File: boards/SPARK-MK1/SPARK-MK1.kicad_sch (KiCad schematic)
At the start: 64 parts, among them J1 Screw_Terminal_01x02, J101 Conn_01x04_Pin, J102 Screw_Terminal_01x02, J103 Screw_Terminal_01x02, J104 Conn_01x04_Pin, J105 Conn_01x04_Pin, J106 Screw_Terminal_01x02, J107 Screw_Terminal_01x02, J108 Conn_01x04_Pin, J109 Conn_01x04_Pin, J110 Conn_01x02_Pin, J111 Conn_01x04_Pin, J112 Conn_01x04_Pin, J2 Screw_Terminal_01x02, J3 Screw_Terminal_01x02, J4 Screw_Terminal_01x02, U1 AD5252BRUZ1, U101 AD5252BRUZ1, U2 Teensy4.1_bare, U5 TPS25947, U6 TPS25947, U7 TPS25947, U8 TPS25947

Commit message: Fixing Footprints, etc
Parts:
- U2: footprint Teensy4.1bare:Teensy41_bare_pins -> Teensy4.1bare:Teensy_4.1
- U5, U6, U7, U8: footprint efuse:VQFN-HR-RPW0010A -> Package_VQFN:VQFN-HR-RPW0010A
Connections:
- no-connect marks 8 -> 37
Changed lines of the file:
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@@
   (junction (at 297.18 138.43) (diameter 0) (color 0 0 0 0)
   )
+  (no_connect (at 110.49 135.89))
+  (no_connect (at 110.49 168.91))
+  (no_connect (at 54.61 151.13))
   (no_connect (at 30.48 43.18))
+  (no_connect (at 110.49 146.05))
+  (no_connect (at 110.49 181.61))
+  (no_connect (at 54.61 163.83))
   (no_connect (at 105.41 41.91))
   (no_connect (at 321.31 97.79))
   (no_connect (at 30.48 45.72))
+  (no_connect (at 110.49 176.53))
+  (no_connect (at 54.61 156.21))
+  (no_connect (at 110.49 158.75))
+  (no_connect (at 110.49 143.51))
+  (no_connect (at 110.49 184.15))
+  (no_connect (at 110.49 179.07))
+  (no_connect (at 54.61 166.37))
+  (no_connect (at 110.49 166.37))
+  (no_connect (at 54.61 171.45))
   (no_connect (at 320.04 41.91))
+  (no_connect (at 110.49 171.45))
+  (no_connect (at 110.49 140.97))
   (no_connect (at 105.41 44.45))
+  (no_connect (at 54.61 148.59))
+  (no_connect (at 110.49 173.99))
   (no_connect (at 320.04 151.13))
   (no_connect (at 318.77 204.47))
+  (no_connect (at 110.49 133.35))
+  (no_connect (at 110.49 156.21))
+  (no_connect (at 54.61 168.91))
+  (no_connect (at 110.49 138.43))
+  (no_connect (at 54.61 184.15))
+  (no_connect (at 110.49 163.83))
+  (no_connect (at 110.49 121.92))
+  (no_connect (at 54.61 158.75))
+  (no_connect (at 110.49 125.73))
+  (no_connect (at 54.61 153.67))
   (wire (pts (xy 318.77 39.37) (xy 320.04 39.37))
     (stroke (width 0) (type default))
@@
       (effects (font (size 1.27 1.27)))
     )
-    (property "Footprint" "efuse:VQFN-HR-RPW0010A" (at 337.82 105.41 0)
+    (property "Footprint" "Package_VQFN:VQFN-HR-RPW0010A" (at 337.82 105.41 0)
       (effects (font (size 1.27 1.27)) hide)
     )
@@
       (effects (font (size 1.27 1.27)))
     )
-    (property "Footprint" "Teensy4.1bare:Teensy41_bare_pins" (at 82.55 194.31 0)
+    (property "Footprint" "Teensy4.1bare:Teensy_4.1" (at 82.55 194.31 0)
       (effects (font (size 1.27 1.27)) hide)
     )
@@
       (effects (font (size 1.27 1.27)))
     )
-    (property "Footprint" "efuse:VQFN-HR-RPW0010A" (at 335.28 212.09 0)
+    (property "Footprint" "Package_VQFN:VQFN-HR-RPW0010A" (at 335.28 212.09 0)
       (effects (font (size 1.27 1.27)) hide)
     )
@@
       (effects (font (size 1.27 1.27)))
     )
-    (property "Footprint" "efuse:VQFN-HR-RPW0010A" (at 336.55 158.75 0)
+    (property "Footprint" "Package_VQFN:VQFN-HR-RPW0010A" (at 336.55 158.75 0)
       (effects (font (size 1.27 1.27)) hide)
     )
@@
       (effects (font (size 1.27 1.27)))
     )
-    (property "Footprint" "efuse:VQFN-HR-RPW0010A" (at 336.55 49.53 0)
+    (property "Footprint" "Package_VQFN:VQFN-HR-RPW0010A" (at 336.55 49.53 0)
       (effects (font (size 1.27 1.27)) hide)
     )

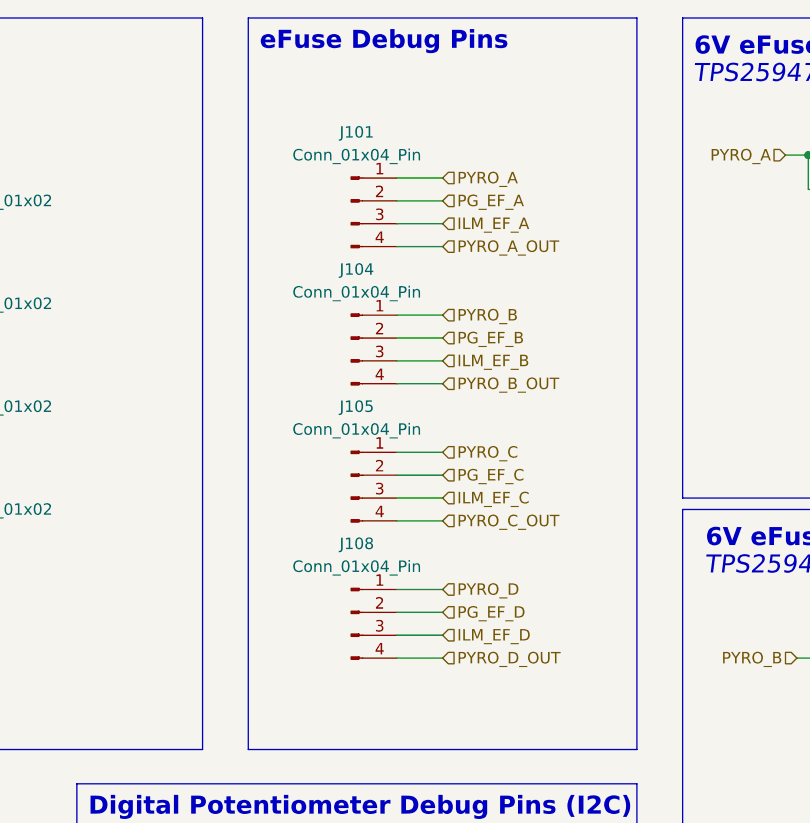
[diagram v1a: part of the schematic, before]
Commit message: Four pins -> three pins
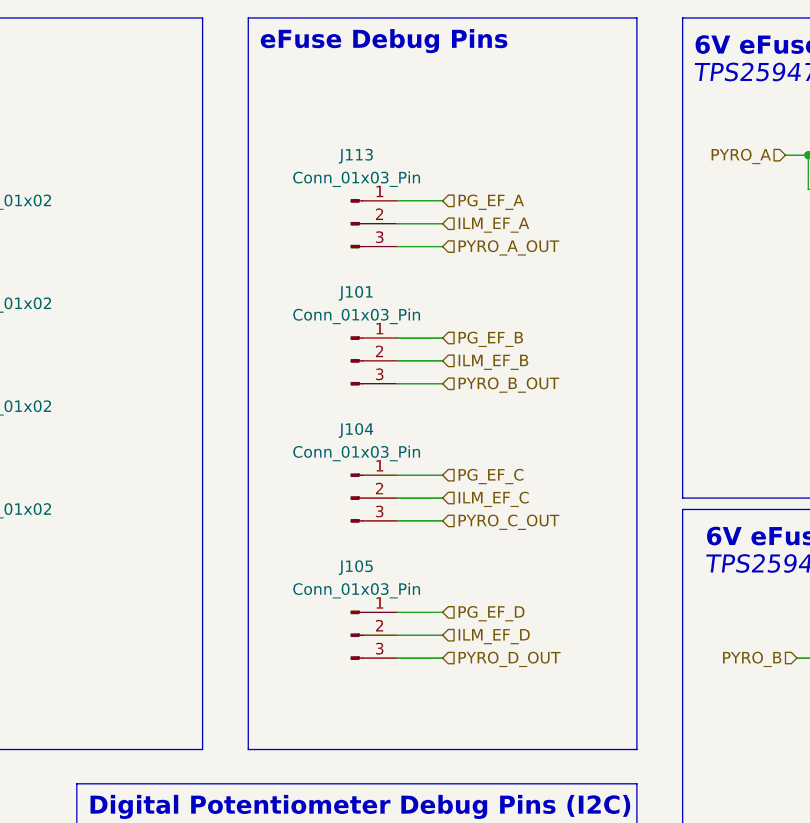
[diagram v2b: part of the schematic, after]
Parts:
- removed J101, J104, J105, J108: Conn_01x04_Pin, Connector_PinHeader_2.54mm:PinHeader_1x04_P2.54mm_Vertical, symbol Connector:Conn_01x04_Pin
- added J101, J104, J105, J113: Conn_01x03_Pin, Connector_PinHeader_2.54mm:PinHeader_1x03_P2.54mm_Vertical, symbol Connector:Conn_01x03_Pin
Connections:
- net B1_A: now also J113.2 (Pin_2)
- net B1_B: now also J104.2 (Pin_2)
- net B3_A: now also J101.2 (Pin_2)
- net B3_B: now also J105.2 (Pin_2)
- net GND: now also J101.3 (Pin_3), J104.3 (Pin_3), J105.3 (Pin_3), J113.3 (Pin_3)
- net PG_EF_A: now also J113.1 (Pin_1)
- net PG_EF_B: now also J101.1 (Pin_1)
- net PG_EF_C: now also J104.1 (Pin_1)
- net PG_EF_D: now also J105.1 (Pin_1)
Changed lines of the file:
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@@
     (stroke (width 0) (type default))
   )
-  (wire (pts (xy 251.46 31.75) (xy 256.54 31.75))
-    (stroke (width 0) (type default))
-  )
   (wire (pts (xy 336.55 46.99) (xy 336.55 53.34))
     (stroke (width 0) (type default))
@@
     (stroke (width 0) (type default))
   )
-  (wire (pts (xy 251.46 77.47) (xy 256.54 77.47))
-    (stroke (width 0) (type default))
-  )
   (wire (pts (xy 384.81 138.43) (xy 392.43 138.43))
     (stroke (width 0) (type default))
@@
     (stroke (width 0) (type default))
   )
-  (wire (pts (xy 251.46 46.99) (xy 256.54 46.99))
-    (stroke (width 0) (type default))
-  )
   (wire (pts (xy 363.22 167.64) (xy 360.68 167.64))
     (stroke (width 0) (type default))
@@
     (stroke (width 0) (type default))
   )
-  (wire (pts (xy 251.46 62.23) (xy 256.54 62.23))
-    (stroke (width 0) (type default))
-  )
   (wire (pts (xy 259.08 115.57) (xy 264.16 115.57))
     (stroke (width 0) (type default))
@@
     (effects (font (size 1.27 1.27)) (justify left))
   )
-  (hierarchical_label "PYRO_D" (shape input) (at 256.54 77.47 0) (fields_autoplaced)
-    (effects (font (size 1.27 1.27)) (justify left))
-  )
   (hierarchical_label "W1_A" (shape bidirectional) (at 354.33 49.53 0) (fields_autoplaced)
     (effects (font (size 1.27 1.27)) (justify left))
@@
     (effects (font (size 1.27 1.27)) (justify left))
   )
-  (hierarchical_label "PYRO_A" (shape input) (at 256.54 31.75 0) (fields_autoplaced)
-    (effects (font (size 1.27 1.27)) (justify left))
-  )
   (hierarchical_label "B1_A" (shape bidirectional) (at 354.33 44.45 0) (fields_autoplaced)
     (effects (font (size 1.27 1.27)) (justify left))
@@
     (effects (font (size 1.27 1.27)) (justify right))
   )
-  (hierarchical_label "PYRO_B" (shape input) (at 256.54 46.99 0) (fields_autoplaced)
-    (effects (font (size 1.27 1.27)) (justify left))
-  )
   (hierarchical_label "PYRO_D_OUT" (shape input) (at 256.54 85.09 0) (fields_autoplaced)
     (effects (font (size 1.27 1.27)) (justify left))
@@
     (effects (font (size 1.27 1.27)) (justify left))
   )
-  (hierarchical_label "PYRO_C" (shape input) (at 256.54 62.23 0) (fields_autoplaced)
-    (effects (font (size 1.27 1.27)) (justify left))
-  )
   (hierarchical_label "PYRO_D" (shape output) (at 181.61 66.04 180) (fields_autoplaced)
     (effects (font (size 1.27 1.27)) (justify right))
@@
     )
   )
+  (symbol (lib_id "Connector:Conn_01x03_Pin") (at 246.38 82.55 0) (unit 1)
+    (in_bom yes) (on_board yes) (dnp no) (fields_autoplaced)
+    (property "Reference" "J105" (at 247.015 74.93 0)
+      (effects (font (size 1.27 1.27)))
+    )
+    (property "Value" "Conn_01x03_Pin" (at 247.015 77.47 0)
+      (effects (font (size 1.27 1.27)))
+    )
+    (property "Footprint" "Connector_PinHeader_2.54mm:PinHeader_1x03_P2.54mm_Vertical" (at 246.38 82.55 0)
+      (effects (font (size 1.27 1.27)) hide)
+    )
+    (property "Datasheet" "~" (at 246.38 82.55 0)
+      (effects (font (size 1.27 1.27)) hide)
+    )
+    (pin "3")
+    (pin "1")
+    (pin "2")
+    (instances
+      (project "SPARK-MK1"
+        (path "/9ed31ef1-850d-4612-a113-88d01cf221f5"
+          (reference "J105") (unit 1)
+        )
+      )
+    )
+  )
   (symbol (lib_id "Device:R_US") (at 367.03 104.14 0) (unit 1)
     (in_bom yes) (on_board yes) (dnp no)
@@
     )
   )
+  (symbol (lib_id "Connector:Conn_01x03_Pin") (at 246.38 52.07 0) (unit 1)
+    (in_bom yes) (on_board yes) (dnp no) (fields_autoplaced)
+    (property "Reference" "J101" (at 247.015 44.45 0)
+      (effects (font (size 1.27 1.27)))
+    )
+    (property "Value" "Conn_01x03_Pin" (at 247.015 46.99 0)
+      (effects (font (size 1.27 1.27)))
+    )
+    (property "Footprint" "Connector_PinHeader_2.54mm:PinHeader_1x03_P2.54mm_Vertical" (at 246.38 52.07 0)
+      (effects (font (size 1.27 1.27)) hide)
+    )
+    (property "Datasheet" "~" (at 246.38 52.07 0)
+      (effects (font (size 1.27 1.27)) hide)
+    )
+    (pin "3")
+    (pin "1")
+    (pin "2")
+    (instances
+      (project "SPARK-MK1"
+        (path "/9ed31ef1-850d-4612-a113-88d01cf221f5"
+          (reference "J101") (unit 1)
+        )
+      )
+    )
+  )
   (symbol (lib_id "Device:R_US") (at 307.34 149.86 0) (unit 1)
     (in_bom yes) (on_board yes) (dnp no)
@@
     )
   )
+  (symbol (lib_id "Connector:Conn_01x03_Pin") (at 246.38 36.83 0) (unit 1)
+    (in_bom yes) (on_board yes) (dnp no) (fields_autoplaced)
+    (property "Reference" "J113" (at 247.015 29.21 0)
+      (effects (font (size 1.27 1.27)))
+    )
+    (property "Value" "Conn_01x03_Pin" (at 247.015 31.75 0)
+      (effects (font (size 1.27 1.27)))
+    )
+    (property "Footprint" "Connector_PinHeader_2.54mm:PinHeader_1x03_P2.54mm_Vertical" (at 246.38 36.83 0)
+      (effects (font (size 1.27 1.27)) hide)
+    )
+    (property "Datasheet" "~" (at 246.38 36.83 0)
+      (effects (font (size 1.27 1.27)) hide)
+    )
+    (pin "3")
+    (pin "1")
+    (pin "2")
+    (instances
+      (project "SPARK-MK1"
+        (path "/9ed31ef1-850d-4612-a113-88d01cf221f5"
+          (reference "J113") (unit 1)
+        )
+      )
+    )
+  )
   (symbol (lib_id "Device:R_US") (at 307.34 40.64 0) (unit 1)
     (in_bom yes) (on_board yes) (dnp no)
@@
     )
   )
+  (symbol (lib_id "Connector:Conn_01x03_Pin") (at 246.38 67.31 0) (unit 1)
+    (in_bom yes) (on_board yes) (dnp no) (fields_autoplaced)
+    (property "Reference" "J104" (at 247.015 59.69 0)
+      (effects (font (size 1.27 1.27)))
+    )
+    (property "Value" "Conn_01x03_Pin" (at 247.015 62.23 0)
+      (effects (font (size 1.27 1.27)))
+    )
+    (property "Footprint" "Connector_PinHeader_2.54mm:PinHeader_1x03_P2.54mm_Vertical" (at 246.38 67.31 0)
+      (effects (font (size 1.27 1.27)) hide)
+    )
+    (property "Datasheet" "~" (at 246.38 67.31 0)
+      (effects (font (size 1.27 1.27)) hide)
+    )
+    (pin "3")
+    (pin "1")
+    (pin "2")
+    (instances
+      (project "SPARK-MK1"
+        (path "/9ed31ef1-850d-4612-a113-88d01cf221f5"
+          (reference "J104") (unit 1)
+        )
+      )
+    )
+  )
   (symbol (lib_id "power:GND") (at 101.6 72.39 0) (unit 1)
     (in_bom yes) (on_board yes) (dnp no) (fields_autoplaced)
@@
     )
   )
-  (symbol (lib_id "Connector:Conn_01x04_Pin") (at 246.38 80.01 0) (unit 1)
-    (in_bom yes) (on_board yes) (dnp no)
-    (property "Reference" "J108" (at 247.015 72.39 0)
-      (effects (font (size 1.27 1.27)))
-    )
-    (property "Value" "Conn_01x04_Pin" (at 247.015 74.93 0)
-      (effects (font (size 1.27 1.27)))
-    )
-    (property "Footprint" "Connector_PinHeader_2.54mm:PinHeader_1x04_P2.54mm_Vertical" (at 246.38 80.01 0)
-      (effects (font (size 1.27 1.27)) hide)
-    )
-    (property "Datasheet" "~" (at 246.38 80.01 0)
-      (effects (font (size 1.27 1.27)) hide)
-    )
-    (pin "1")
-    (pin "4")
-    (pin "2")
-    (pin "3")
-    (instances
-      (project "SPARK-MK1"
-        (path "/9ed31ef1-850d-4612-a113-88d01cf221f5"
-          (reference "J108") (unit 1)
-        )
-      )
-    )
-  )
-  (symbol (lib_id "Connector:Conn_01x04_Pin") (at 246.38 49.53 0) (unit 1)
-    (in_bom yes) (on_board yes) (dnp no)
-    (property "Reference" "J104" (at 247.015 41.91 0)
-      (effects (font (size 1.27 1.27)))
-    )
-    (property "Value" "Conn_01x04_Pin" (at 247.015 44.45 0)
-      (effects (font (size 1.27 1.27)))
-    )
-    (property "Footprint" "Connector_PinHeader_2.54mm:PinHeader_1x04_P2.54mm_Vertical" (at 246.38 49.53 0)
-      (effects (font (size 1.27 1.27)) hide)
-    )
-    (property "Datasheet" "~" (at 246.38 49.53 0)
-      (effects (font (size 1.27 1.27)) hide)
-    )
-    (pin "1")
-    (pin "4")
-    (pin "2")
-    (pin "3")
-    (instances
-      (project "SPARK-MK1"
-        (path "/9ed31ef1-850d-4612-a113-88d01cf221f5"
-          (reference "J104") (unit 1)
-        )
-      )
-    )
-  )
   (symbol (lib_id "Connector:Screw_Terminal_01x02") (at 368.3 165.1 0) (unit 1)
     (in_bom yes) (on_board yes) (dnp no) (fields_autoplaced)
@@
     )
   )
-  (symbol (lib_id "Connector:Conn_01x04_Pin") (at 246.38 64.77 0) (unit 1)
-    (in_bom yes) (on_board yes) (dnp no)
-    (property "Reference" "J105" (at 247.015 57.15 0)
-      (effects (font (size 1.27 1.27)))
-    )
-    (property "Value" "Conn_01x04_Pin" (at 247.015 59.69 0)
-      (effects (font (size 1.27 1.27)))
-    )
-    (property "Footprint" "Connector_PinHeader_2.54mm:PinHeader_1x04_P2.54mm_Vertical" (at 246.38 64.77 0)
-      (effects (font (size 1.27 1.27)) hide)
-    )
-    (property "Datasheet" "~" (at 246.38 64.77 0)
-      (effects (font (size 1.27 1.27)) hide)
-    )
-    (pin "1")
-    (pin "4")
-    (pin "2")
-    (pin "3")
-    (instances
-      (project "SPARK-MK1"
-        (path "/9ed31ef1-850d-4612-a113-88d01cf221f5"
-          (reference "J105") (unit 1)
-        )
-      )
-    )
-  )
   (symbol (lib_id "Device:R_US") (at 365.76 48.26 0) (unit 1)
     (in_bom yes) (on_board yes) (dnp no)
@@
         )
       )
-    )
-  )
-  (symbol (lib_id "Connector:Conn_01x04_Pin") (at 246.38 34.29 0) (unit 1)
-    (in_bom yes) (on_board yes) (dnp no)
-    (property "Reference" "J101" (at 247.015 26.67 0)
-      (effects (font (size 1.27 1.27)))
-    )
-    (property "Value" "Conn_01x04_Pin" (at 247.015 29.21 0)
-      (effects (font (size 1.27 1.27)))
-    )
-    (property "Footprint" "Connector_PinHeader_2.54mm:PinHeader_1x04_P2.54mm_Vertical" (at 246.38 34.29 0)
-      (effects (font (size 1.27 1.27)) hide)
-    )
-    (property "Datasheet" "~" (at 246.38 34.29 0)
-      (effects (font (size 1.27 1.27)) hide)
-    )
-    (pin "1")
-    (pin "4")
-    (pin "2")
-    (pin "3")
-    (instances
-      (project "SPARK-MK1"
-        (path "/9ed31ef1-850d-4612-a113-88d01cf221f5"
-          (reference "J101") (unit 1)
-        )
-      )

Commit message: fixing small things and adding footprints to PCB
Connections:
- net GND: no longer C11.1, C12.1, C7.1, C8.1, J1.1 (Pin_1), J101.3 (Pin_3), J104.3 (Pin_3), J105.3 (Pin_3), J113.3 (Pin_3), J2.1 (Pin_1), J3.1 (Pin_1), J4.1 (Pin_1), R23.2, R24.2, R35.2, R36.2, U5.6 (OUT), U6.6 (OUT), U7.6 (OUT), U8.6 (OUT)
- new net PYRO_A_OUT: C7.1, J1.1 (Pin_1), J113.3 (Pin_3), R23.2, U5.6 (OUT)
- new net PYRO_B_OUT: C8.1, J101.3 (Pin_3), J2.1 (Pin_1), R24.2, U6.6 (OUT)
- new net PYRO_C_OUT: C11.1, J104.3 (Pin_3), J3.1 (Pin_1), R35.2, U7.6 (OUT)
- new net PYRO_D_OUT: C12.1, J105.3 (Pin_3), J4.1 (Pin_1), R36.2, U8.6 (OUT)
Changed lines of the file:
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@@
   (junction (at 308.61 88.9) (diameter 0) (color 0 0 0 0)
   )
-  (junction (at 377.19 109.22) (diameter 0) (color 0 0 0 0)
-  )
   (junction (at 335.28 215.9) (diameter 0) (color 0 0 0 0)
   )
-  (junction (at 375.92 162.56) (diameter 0) (color 0 0 0 0)
-  )
   (junction (at 339.09 162.56) (diameter 0) (color 0 0 0 0)
   )
@@
   (junction (at 318.77 162.56) (diameter 0) (color 0 0 0 0)
   )
-  (junction (at 374.65 215.9) (diameter 0) (color 0 0 0 0)
-  )
   (junction (at 354.33 109.22) (diameter 0) (color 0 0 0 0)
   )
@@
   (junction (at 374.65 195.58) (diameter 0) (color 0 0 0 0)
   )
-  (junction (at 384.81 138.43) (diameter 0) (color 0 0 0 0)
-  )
-  (junction (at 383.54 29.21) (diameter 0) (color 0 0 0 0)
-  )
   (junction (at 365.76 33.02) (diameter 0) (color 0 0 0 0)
   )
@@
   (junction (at 309.88 162.56) (diameter 0) (color 0 0 0 0)
   )
-  (junction (at 386.08 85.09) (diameter 0) (color 0 0 0 0)
-  )
-  (junction (at 375.92 53.34) (diameter 0) (color 0 0 0 0)
-  )
   (junction (at 351.79 198.12) (diameter 0) (color 0 0 0 0)
-  )
-  (junction (at 383.54 191.77) (diameter 0) (color 0 0 0 0)
   )
   (junction (at 367.03 109.22) (diameter 0) (color 0 0 0 0)
@@
     (stroke (width 0) (type default))
   )
-  (wire (pts (xy 386.08 85.09) (xy 392.43 85.09))
+  (wire (pts (xy 377.19 85.09) (xy 392.43 85.09))
     (stroke (width 0) (type default))
   )
@@
     (stroke (width 0) (type default))
   )
-  (wire (pts (xy 384.81 138.43) (xy 384.81 162.56))
-    (stroke (width 0) (type default))
-  )
   (wire (pts (xy 370.84 114.3) (xy 370.84 115.57))
     (stroke (width 0) (type default))
@@
     (stroke (width 0) (type default))
   )
-  (wire (pts (xy 374.65 191.77) (xy 383.54 191.77))
-    (stroke (width 0) (type default))
-  )
   (wire (pts (xy 353.06 158.75) (xy 353.06 162.56))
     (stroke (width 0) (type default))
@@
     (stroke (width 0) (type default))
   )
-  (wire (pts (xy 383.54 215.9) (xy 374.65 215.9))
-    (stroke (width 0) (type default))
-  )
   (wire (pts (xy 190.5 143.51) (xy 198.12 143.51))
     (stroke (width 0) (type default))
@@
     (stroke (width 0) (type default))
   )
-  (wire (pts (xy 383.54 29.21) (xy 392.43 29.21))
-    (stroke (width 0) (type default))
-  )
   (wire (pts (xy 350.52 195.58) (xy 364.49 195.58))
     (stroke (width 0) (type default))
@@
     (stroke (width 0) (type default))
   )
-  (wire (pts (xy 386.08 109.22) (xy 377.19 109.22))
-    (stroke (width 0) (type default))
-  )
   (wire (pts (xy 318.77 53.34) (xy 336.55 53.34))
     (stroke (width 0) (type default))
@@
     (stroke (width 0) (type default))
   )
-  (wire (pts (xy 377.19 85.09) (xy 386.08 85.09))
-    (stroke (width 0) (type default))
-  )
   (wire (pts (xy 110.49 151.13) (xy 116.84 151.13))
     (stroke (width 0) (type default))
@@
     (stroke (width 0) (type default))
   )
-  (wire (pts (xy 383.54 191.77) (xy 392.43 191.77))
+  (wire (pts (xy 374.65 191.77) (xy 392.43 191.77))
     (stroke (width 0) (type default))
   )
@@
     (stroke (width 0) (type default))
   )
-  (wire (pts (xy 383.54 191.77) (xy 383.54 215.9))
-    (stroke (width 0) (type default))
-  )
   (wire (pts (xy 307.34 53.34) (xy 309.88 53.34))
     (stroke (width 0) (type default))
@@
     (stroke (width 0) (type default))
   )
-  (wire (pts (xy 384.81 138.43) (xy 392.43 138.43))
-    (stroke (width 0) (type default))
-  )
   (wire (pts (xy 351.79 142.24) (xy 365.76 142.24))
     (stroke (width 0) (type default))
@@
     (stroke (width 0) (type default))
   )
-  (wire (pts (xy 383.54 29.21) (xy 383.54 53.34))
-    (stroke (width 0) (type default))
-  )
   (wire (pts (xy 354.33 105.41) (xy 356.87 105.41))
     (stroke (width 0) (type default))
@@
     (stroke (width 0) (type default))
   )
-  (wire (pts (xy 386.08 85.09) (xy 386.08 109.22))
-    (stroke (width 0) (type default))
-  )
   (wire (pts (xy 377.19 85.09) (xy 377.19 88.9))
     (stroke (width 0) (type default))
@@
     (stroke (width 0) (type default))
   )
-  (wire (pts (xy 383.54 53.34) (xy 375.92 53.34))
-    (stroke (width 0) (type default))
-  )
   (wire (pts (xy 306.07 142.24) (xy 307.34 142.24))
     (stroke (width 0) (type default))
@@
     (stroke (width 0) (type default))
   )
-  (wire (pts (xy 375.92 29.21) (xy 383.54 29.21))
+  (wire (pts (xy 375.92 29.21) (xy 392.43 29.21))
     (stroke (width 0) (type default))
   )
@@
     (stroke (width 0) (type default))
   )
-  (wire (pts (xy 375.92 138.43) (xy 384.81 138.43))
+  (wire (pts (xy 375.92 138.43) (xy 392.43 138.43))
     (stroke (width 0) (type default))
   )
@@
     (stroke (width 0) (type default))
   )
-  (wire (pts (xy 384.81 162.56) (xy 375.92 162.56))
-    (stroke (width 0) (type default))
-  )
